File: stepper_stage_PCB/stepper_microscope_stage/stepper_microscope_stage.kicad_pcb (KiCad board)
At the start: 2 copper layers, 131.5 x 158.8 mm, 22 parts, among them J1 Conn_01x04_Socket

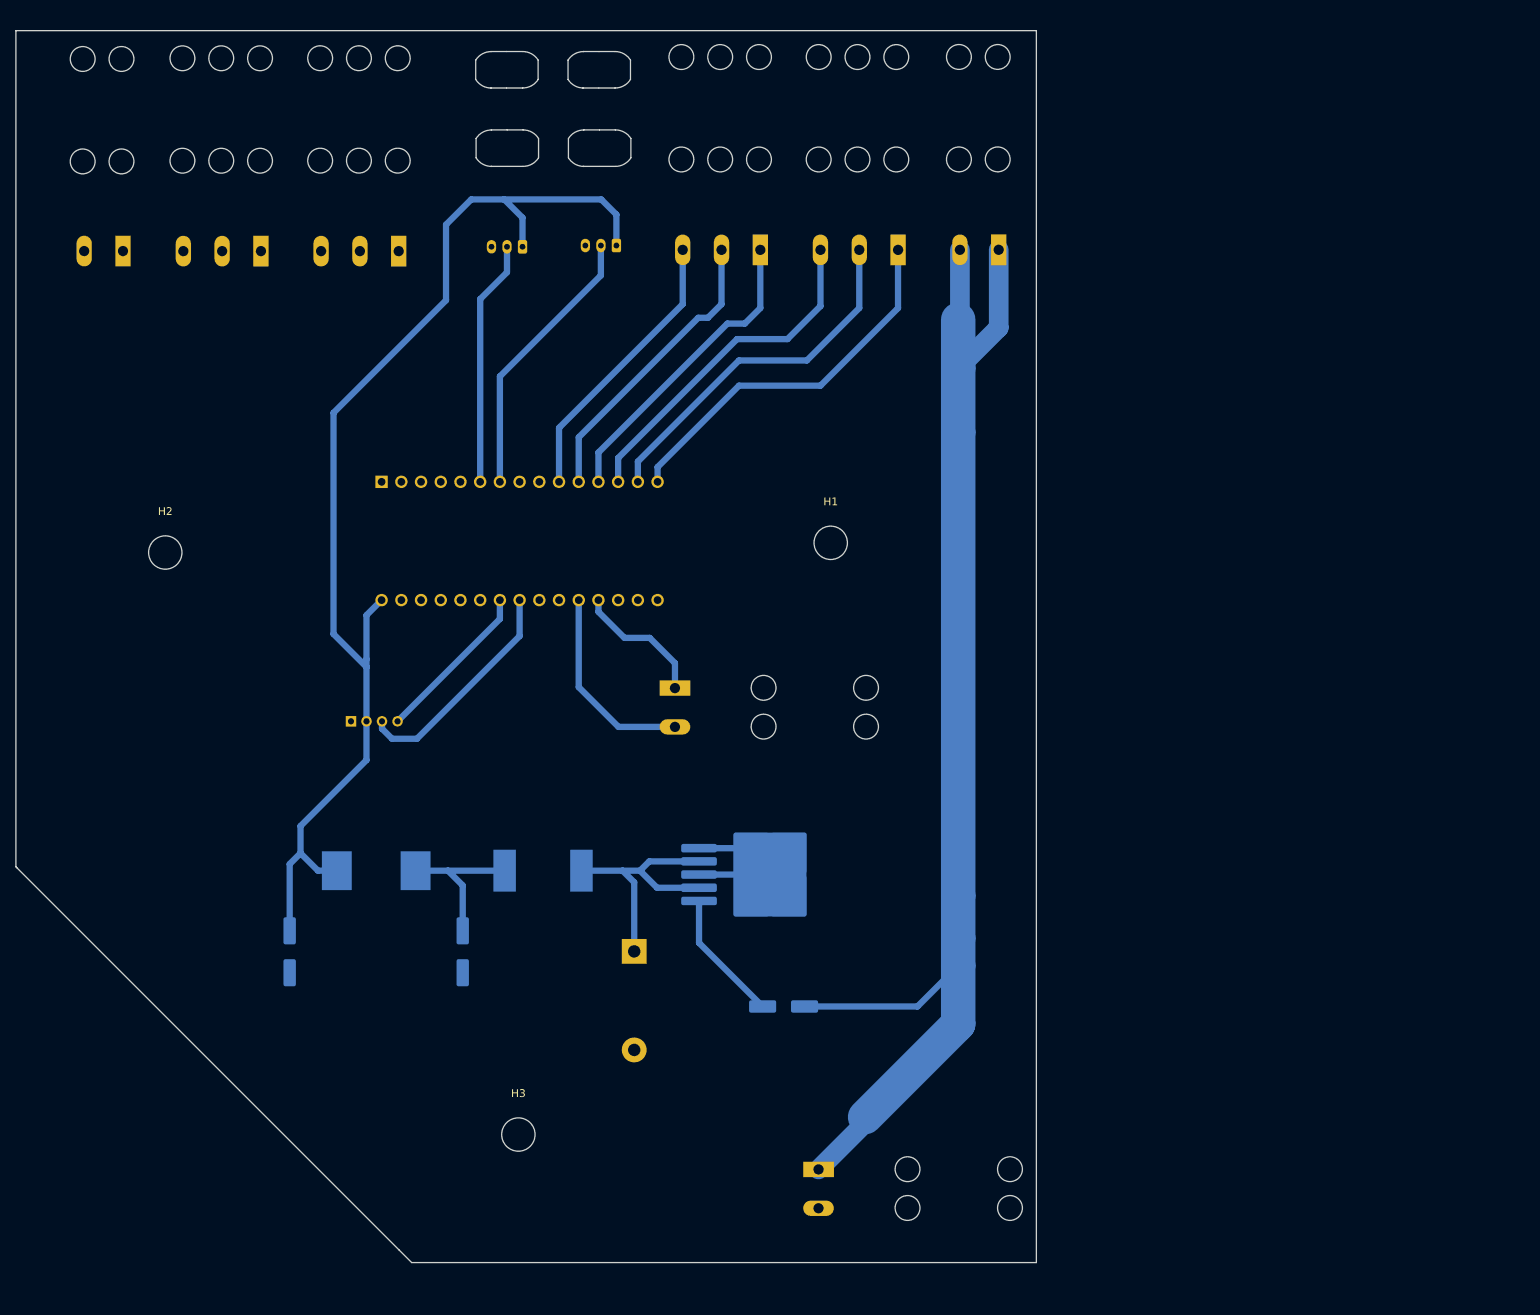
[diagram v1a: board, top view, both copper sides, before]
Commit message: Route GND of +24v net.
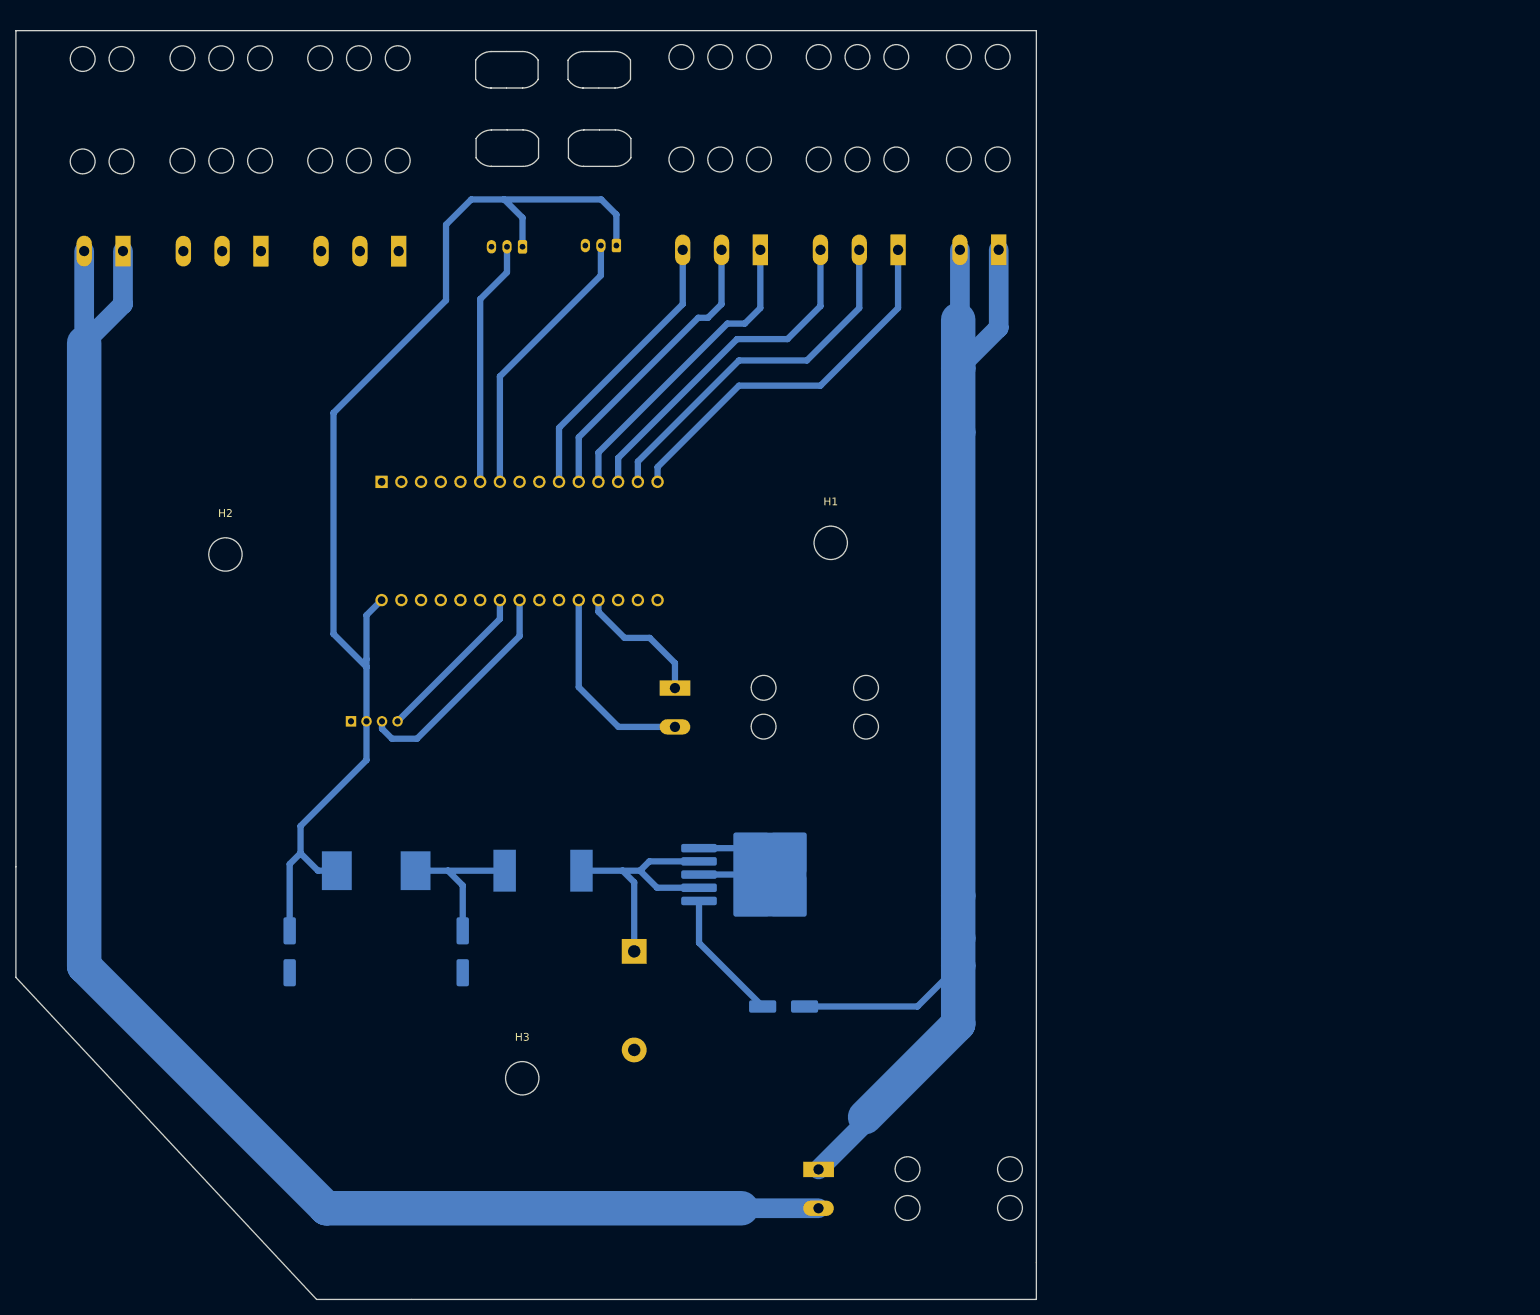
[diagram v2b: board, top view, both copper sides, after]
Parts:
- moved H2 7.75 mm to (54.5, 84.5)
- moved H3 7.27 mm to (92.8, 152.0)
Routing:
- net GND: track 16.9 -> 230.5 mm
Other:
- board size 131.5 x 158.8 mm -> 131.5 x 163.5 mm
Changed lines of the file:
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@@
   )
   (footprint "MountingHole:MountingHole_4.3mm_M4" (layer "F.Cu")
-    (at 46.75 84.25)
+    (at 54.5 84.5)
     (descr "Mounting Hole 4.3mm, no annular, M4")
     (tags "mounting hole 4.3mm no annular m4")
@@
   )
   (footprint "MountingHole:MountingHole_4.3mm_M4" (layer "F.Cu")
-    (at 92.25 159.25)
+    (at 92.75 152)
     (descr "Mounting Hole 4.3mm, no annular, M4")
     (tags "mounting hole 4.3mm no annular m4")
@@
   (gr_circle (center 71.705 20.550816) (end 71.705 22.150816)
     (stroke (width 0.1) (type default)) (fill none) (layer "Edge.Cuts"))
-  (gr_line (start 27.5 124.75) (end 27.625 124.875)
-    (stroke (width 0.1) (type default)) (layer "Edge.Cuts"))
   (gr_circle (center 41.105 20.650816) (end 41.105 22.250816)
     (stroke (width 0.1) (type default)) (fill none) (layer "Edge.Cuts"))
@@
   (gr_circle (center 66.705 33.750816) (end 66.705 35.350816)
     (stroke (width 0.1) (type default)) (fill none) (layer "Edge.Cuts"))
-  (gr_line (start 27.625 124.875) (end 76.875 174.125)
-    (stroke (width 0.1) (type default)) (layer "Edge.Cuts"))
   (gr_line (start 92.804998 24.39) (end 90.754998 24.39)
     (stroke (width 0.1) (type default)) (layer "Edge.Cuts"))
@@
   (gr_line (start 159 17) (end 27.5 17)
     (stroke (width 0.1) (type default)) (layer "Edge.Cuts"))
+  (gr_line (start 159 175.75) (end 159 180.5)
+    (stroke (width 0.1) (type default)) (layer "Edge.Cuts"))
   (gr_circle (center 118.255 33.6) (end 118.255 35.2)
     (stroke (width 0.1) (type default)) (fill none) (layer "Edge.Cuts"))
@@
   (gr_circle (center 48.96 20.560816) (end 48.96 22.160816)
     (stroke (width 0.1) (type default)) (fill none) (layer "Edge.Cuts"))
-  (gr_line (start 78.5 175.75) (end 159 175.75)
+  (gr_line (start 78.5 180.5) (end 159 180.5)
     (stroke (width 0.1) (type default)) (layer "Edge.Cuts"))
   (gr_line (start 98.70141 30.899912) (end 98.70141 33.390908)
@@
   (gr_arc (start 92.804998 19.69) (mid 93.944206 19.984588) (end 94.797794 20.794502)
     (stroke (width 0.1) (type default)) (layer "Edge.Cuts"))
-  (gr_line (start 78.5 175.75) (end 76.875 174.125)
+  (gr_line (start 27.5 124.75) (end 27.5 139)
     (stroke (width 0.1) (type default)) (layer "Edge.Cuts"))
   (gr_circle (center 36.105 20.650816) (end 36.105 22.250816)
@@
   (gr_circle (center 149.02 20.39) (end 149.02 21.99)
     (stroke (width 0.1) (type default)) (fill none) (layer "Edge.Cuts"))
+  (gr_line (start 78.5 180.5) (end 66.25 180.5)
+    (stroke (width 0.1) (type default)) (layer "Edge.Cuts"))
   (gr_circle (center 48.96 33.760816) (end 48.96 35.360816)
     (stroke (width 0.1) (type default)) (fill none) (layer "Edge.Cuts"))
   (gr_circle (center 137.05 106.685) (end 135.45 106.685)
     (stroke (width 0.1) (type default)) (fill none) (layer "Edge.Cuts"))
+  (gr_line (start 66.25 180.5) (end 27.5 139)
+    (stroke (width 0.1) (type default)) (layer "Edge.Cuts"))
   (gr_arc (start 94.797794 23.285498) (mid 93.944206 24.095415) (end 92.804998 24.39)
     (stroke (width 0.1) (type default)) (layer "Edge.Cuts"))
@@
     (stroke (width 0.1) (type default)) (fill none) (layer "Edge.Cuts"))
   (segment (start 115.527856 122.35) (end 121.627856 122.35) (width 0.8128) (layer "B.Cu") (net 1))
+  (segment (start 130.927856 168.75) (end 121 168.75) (width 2.54) (layer "B.Cu") (net 1))
+  (segment (start 67.5 168.75) (end 121 168.75) (width 4.445) (layer "B.Cu") (net 1))
   (segment (start 115.527856 125.75) (end 124.677856 125.75) (width 0.8128) (layer "B.Cu") (net 1))
+  (segment (start 36.297856 137.547856) (end 67.5 168.75) (width 4.445) (layer "B.Cu") (net 1))
+  (segment (start 36.297856 45.400816) (end 36.297856 57.25) (width 2.54) (layer "B.Cu") (net 1))
   (segment (start 77.387856 44.850816) (end 76.827856 45.410816) (width 0.8128) (layer "B.Cu") (net 1))
+  (segment (start 36.297856 57.25) (end 36.297856 137.547856) (width 4.445) (layer "B.Cu") (net 1))
+  (segment (start 41.297856 52.25) (end 36.297856 57.25) (width 2.54) (layer "B.Cu") (net 1))
   (segment (start 121.627856 122.35) (end 122.252856 122.975) (width 0.8128) (layer "B.Cu") (net 1))
+  (segment (start 41.297856 45.400816) (end 41.297856 52.25) (width 2.54) (layer "B.Cu") (net 1))
   (segment (start 87.327856 51.6) (end 87.327856 75.14) (width 0.8128) (layer "B.Cu") (net 2))
   (segment (start 90.782856 48.145) (end 87.327856 51.6) (width 0.8128) (layer "B.Cu") (net 2))
@@
   (segment (start 148.927856 137.5) (end 148.927856 145) (width 4.445) (layer "B.Cu") (net 8))
   (segment (start 148.927856 128.5) (end 148.927856 133.95) (width 4.445) (layer "B.Cu") (net 8))
-  (segment (start 148.942856 68.75) (end 148.927856 68.765) (width 2.54) (layer "B.Cu") (net 8))
   (segment (start 149.147856 45.24) (end 149.147856 54.03) (width 2.54) (layer "B.Cu") (net 8))
   (segment (start 148.927856 145) (end 136.927856 157) (width 4.445) (layer "B.Cu") (net 8))
@@
   (segment (start 90.477856 125.25) (end 83.177856 125.25) (width 0.8128) (layer "B.Cu") (net 34))
   (segment (start 83.177856 125.25) (end 79.002856 125.25) (width 0.8128) (layer "B.Cu") (net 34))
-  (group "" (id 3310a3ea-2624-4f4d-a3cd-e07baa8afcf1)
-    (members
-      3ace4c3b-5bfb-4828-83ca-a876c654b692
-      a2ae76d9-5d78-4689-a815-65280d9491b0
-    )
-  )
-  (group "" (id 3ace4c3b-5bfb-4828-83ca-a876c654b692)
-    (members
-      a240af5a-43f9-4e60-af93-56eab7a67f74
-      db321c74-df15-4aa1-b4f4-accd90a23791
-    )
-  )
   (group "" (id 4ed7ead6-4afd-4d0d-82ef-4572ed372aef)
     (members
@@
     )
   )
-  (group "" (id 585f3644-c33c-4891-86a5-9d6e487a48d9)
-    (members
-      3310a3ea-2624-4f4d-a3cd-e07baa8afcf1
-      7c87d932-be27-4215-bb8f-77a6dbfe07aa
-    )
-  )
   (group "" (id 688c4028-da51-45e8-9897-dc7c87934496)
     (members
@@
     )
   )
-  (group "" (id 745c33f6-2298-4318-9be5-fee8dce6d6cc)
-    (members
-      32bc1a6d-9b38-4397-99f8-3a40a06850fd
-      8c680e07-0dd1-4f3e-8c5e-a115e9d6166f
-      8ce0bd46-23d6-476b-aa8a-5f90b55c675e
-      d05df33a-7517-4374-8c38-9c14478c521e
-      efee18e6-0496-4d49-8bec-2e0c16bb6713
-    )
-  )
-  (group "" (id a240af5a-43f9-4e60-af93-56eab7a67f74)
-    (members
-      10222423-15a5-4abe-a8e3-7a63130a229a
-      26760fc3-1749-417c-9e0b-6af1d6b1ade6
-      868da41c-75ca-45ca-ada3-66d2906f7364
-      86fab09c-78a3-4887-a530-fa9022eaa816
-      c3e1c803-34c9-4b8d-a77d-f778b98aeb70
-    )
-  )
   (group "" (id d05df33a-7517-4374-8c38-9c14478c521e)
     (members
@@
     )
   )
-  (group "" (id db321c74-df15-4aa1-b4f4-accd90a23791)
-    (members
-      6a699131-cd7d-4b5e-b218-4b9e5266cc9f
-      745c33f6-2298-4318-9be5-fee8dce6d6cc
-      7c5decbb-acff-4096-a11f-acbd98735516
-      8b51218e-df1b-4776-944a-bc83bc8c61ff
-      b3445126-1ebc-434f-979b-1b4c3c36506d
-    )
-  )

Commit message: Final 90%
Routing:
- net GND: track 230.5 -> 16.9 mm
- added copper zone on B.Cu, net GND
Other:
- outline, holes or cut-outs redrawn
